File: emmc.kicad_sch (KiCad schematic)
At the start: 5 parts

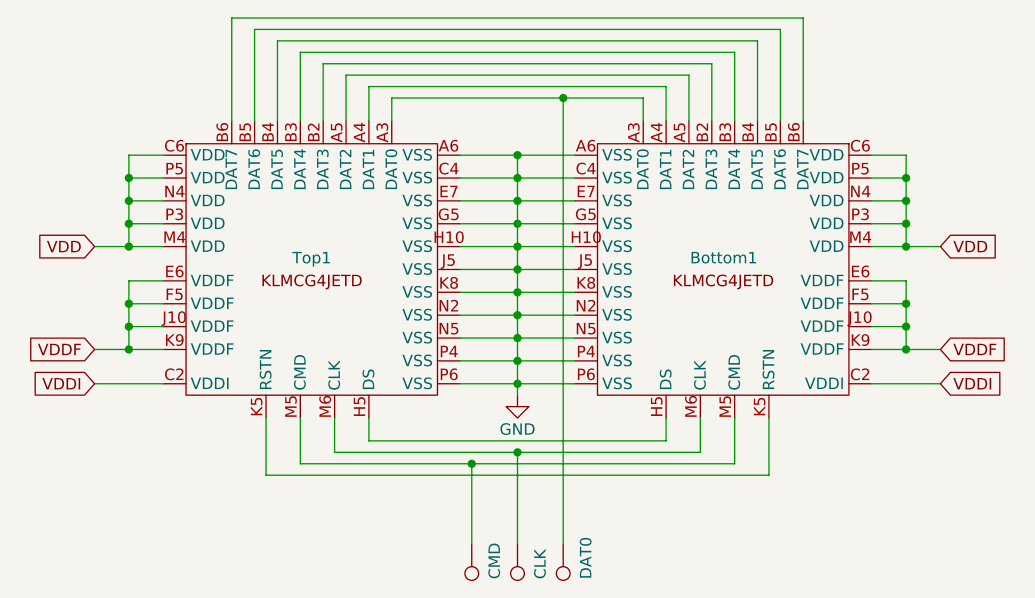
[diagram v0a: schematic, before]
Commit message: Revision: * Change background plane to hatched mode. This is hopefully could reduce the 'bending' pcb, when heated. * All pin will be shown. Hopefully it will make the 'orientation alignment' worked.
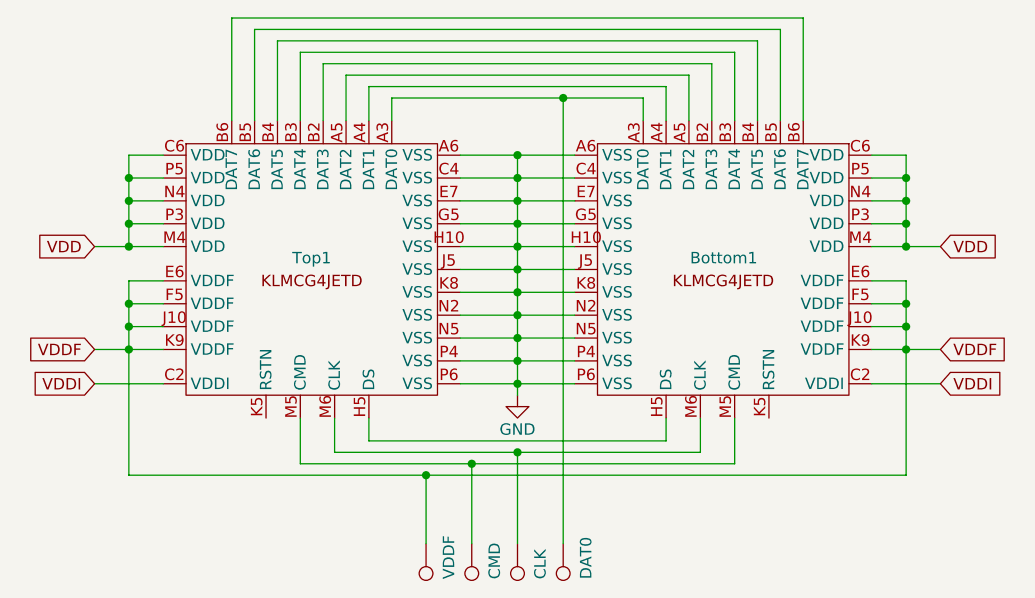
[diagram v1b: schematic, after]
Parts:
- added SP4: VDDF, SniffPoint:VDDF, symbol SniffPoint:DAT0
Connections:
- net VDDF: now also SP4.DAT0
- net at Bottom1.K5 (RSTN): no longer Top1.K5 (RSTN)
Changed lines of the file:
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@@
   (junction (at 133.35 53.34) (diameter 0) (color 0 0 0 0)
   )
+  (junction (at 123.19 88.9) (diameter 0) (color 0 0 0 0)
+  )
   (junction (at 90.17 69.85) (diameter 0) (color 0 0 0 0)
   )
@@
     (stroke (width 0) (type default))
   )
+  (wire (pts (xy 123.19 88.9) (xy 123.19 96.52))
+    (stroke (width 0) (type default))
+  )
   (wire (pts (xy 90.17 58.42) (xy 90.17 60.96))
     (stroke (width 0) (type default))
   )
-  (wire (pts (xy 105.41 88.9) (xy 161.29 88.9))
-    (stroke (width 0) (type default))
-  )
   (wire (pts (xy 113.03 82.55) (xy 113.03 86.36))
     (stroke (width 0) (type default))
@@
     (stroke (width 0) (type default))
   )
-  (wire (pts (xy 161.29 82.55) (xy 161.29 88.9))
-    (stroke (width 0) (type default))
-  )
   (wire (pts (xy 133.35 55.88) (xy 139.7 55.88))
     (stroke (width 0) (type default))
@@
     (stroke (width 0) (type default))
   )
+  (wire (pts (xy 176.53 74.93) (xy 176.53 88.9))
+    (stroke (width 0) (type default))
+  )
   (wire (pts (xy 90.17 55.88) (xy 90.17 58.42))
     (stroke (width 0) (type default))
@@
     (stroke (width 0) (type default))
   )
-  (wire (pts (xy 105.41 82.55) (xy 105.41 88.9))
-    (stroke (width 0) (type default))
-  )
   (wire (pts (xy 149.86 85.09) (xy 149.86 82.55))
     (stroke (width 0) (type default))
@@
     (stroke (width 0) (type default))
   )
+  (wire (pts (xy 90.17 74.93) (xy 90.17 88.9))
+    (stroke (width 0) (type default))
+  )
   (wire (pts (xy 127 76.2) (xy 133.35 76.2))
     (stroke (width 0) (type default))
@@
     (stroke (width 0) (type default))
   )
+  (wire (pts (xy 123.19 88.9) (xy 176.53 88.9))
+    (stroke (width 0) (type default))
+  )
   (wire (pts (xy 127 71.12) (xy 133.35 71.12))
     (stroke (width 0) (type default))
@@
   )
   (wire (pts (xy 133.35 80.01) (xy 133.35 78.74))
+    (stroke (width 0) (type default))
+  )
+  (wire (pts (xy 90.17 88.9) (xy 123.19 88.9))
     (stroke (width 0) (type default))
   )
@@
         )
       )
+    )
+  )
+  (symbol (lib_id "SniffPoint:DAT0") (at 123.19 96.52 180) (unit 1)
+    (in_bom yes) (on_board yes) (dnp no)
+    (property "Reference" "SP4" (at 125.73 99.187 0)
+      (effects (font (size 1.27 1.27)) (justify right) hide)
+    )
+    (property "Value" "VDDF" (at 125.73 100.457 90)
+      (effects (font (size 1.27 1.27)) (justify right))
+    )
+    (property "Footprint" "SniffPoint:VDDF" (at 118.11 96.52 0)
+      (effects (font (size 1.27 1.27)) hide)
+    )
+    (property "Datasheet" "~" (at 118.11 96.52 0)
+      (effects (font (size 1.27 1.27)) hide)
+    )
+    (pin "DAT0")
+    (instances
+      (project "emmc"
+        (path "/a0d6ba26-adcf-4d44-b30b-17c9118198a6"
+          (reference "SP4") (unit 1)
+        )
+      )
